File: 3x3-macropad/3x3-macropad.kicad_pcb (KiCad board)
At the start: 2 copper layers, 79.3 x 79.3 mm, 40 parts, among them SW1 SW_Push, SW2 RotaryEncoder_Switch, U1 ATmega32U4-A, Y1 16MHz

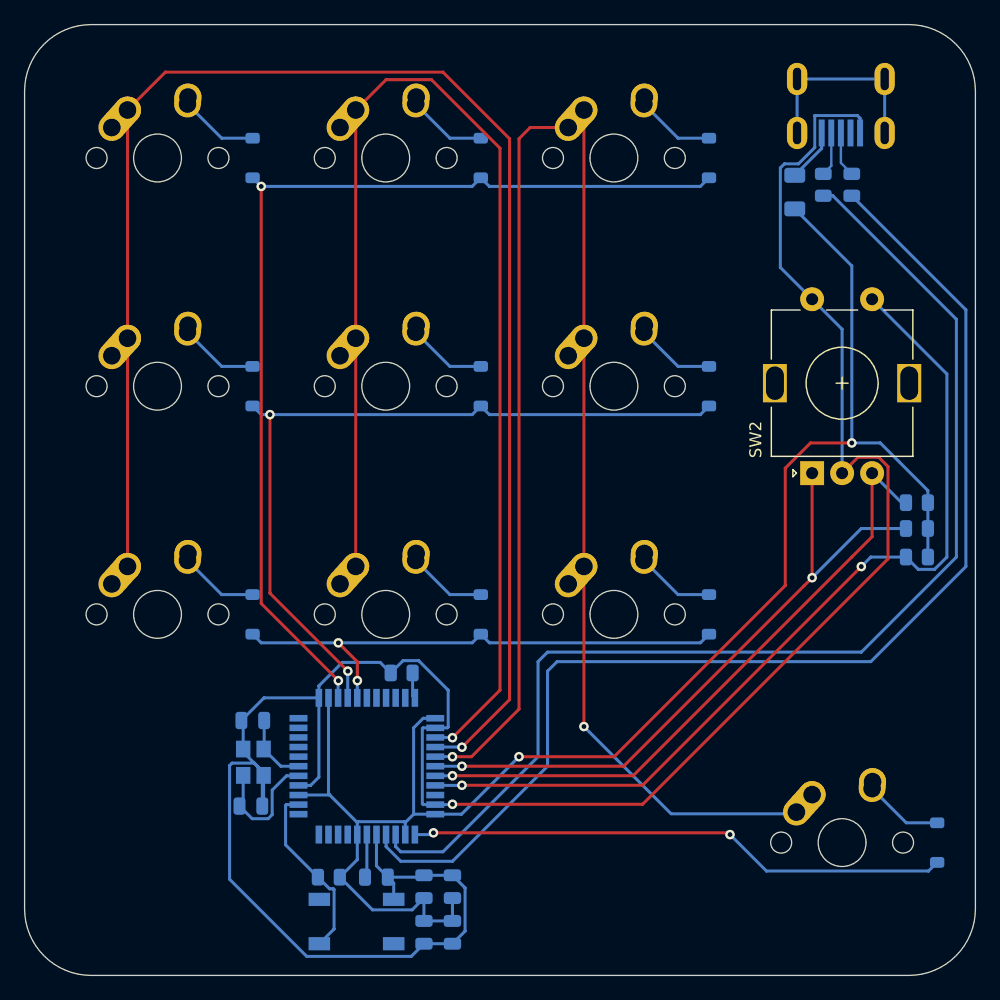
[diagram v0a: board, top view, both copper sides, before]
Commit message: resized 3x3, readied for export to jlcpcb
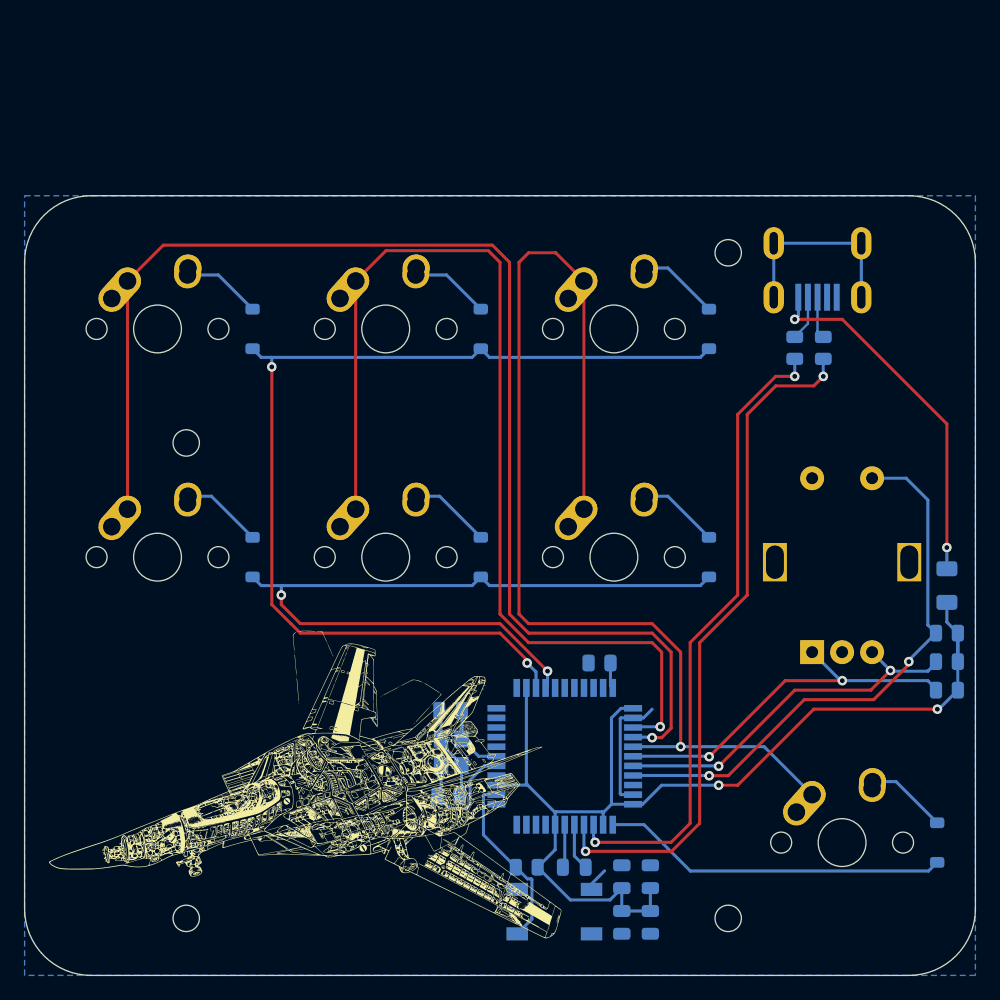
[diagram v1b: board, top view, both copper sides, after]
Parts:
- removed D7, D8, D9: SOD_123, Diode_SMD:D_SOD-123
- removed MX7, MX8, MX9: MX-NoLED, MX_Alps_Hybrid:MX-1U-NoLED
- added G***: LOGO, LOGO, F.Cu at (111.0, 107.8)
- added REF**: MountingHole_2.2mm_M2, MountingHole:MountingHole_2.2mm_M2, F.Cu at (145.9, 118.1)
- added REF**: MountingHole_2.2mm_M2, MountingHole:MountingHole_2.2mm_M2, F.Cu at (145.9, 62.6)
- added REF**: MountingHole_2.2mm_M2, MountingHole:MountingHole_2.2mm_M2, F.Cu at (100.7, 118.1)
- added REF**: MountingHole_2.2mm_M2, MountingHole:MountingHole_2.2mm_M2, F.Cu at (100.7, 78.5)
- moved F1 35.2 mm to (164.1, 90.4)
- moved C2 16.5 mm to (139.4, 114.6)
- moved C7 16.5 mm to (139.4, 118.5)
- moved R4 16.5 mm to (135.1, 96.8)
- moved C1 16.5 mm to (137.0, 114.6)
- moved C3 16.5 mm to (137.0, 118.5)
- moved C4 16.5 mm to (122.7, 100.8)
- moved C5 16.5 mm to (122.6, 107.9)
- moved C6 16.5 mm to (133.0, 113.9)
- moved R3 16.5 mm to (129.1, 113.9)
- moved SW1 16.5 mm to (131.4, 117.6)
- moved Y1 16.5 mm to (122.8, 104.3)
- moved U1 16.5 mm to (132.2, 104.6)
- moved SW2 14.9 mm to (152.9, 95.9)
- moved D1 14.3 mm to (106.2, 69.0)
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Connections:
- D10 pad 1: ROW3 -> ROW2
- U1 pad 1: ROW3 -> ROW2
- U1 pad 27: ROW2 -> unconnected-(U1-PD7-Pad27)
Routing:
- net GND: track 203.6 -> 24.9 mm, vias 1 -> 0
- net +5V: track 139.4 -> 92.2 mm
- net ROW3: track 45.2 -> 0.00 mm, vias 2 -> 0
- net Net-(U1-D-): track 97.9 -> 53.4 mm, vias 0 -> 2
- net COL2: track 142.9 -> 100.3 mm, vias 2 -> 1
- net Net-(U1-D+): track 99.5 -> 57.6 mm, vias 0 -> 2
- net ENCBTN: track 75.5 -> 47.2 mm
- net VCC: track 4.46 -> 30.3 mm, vias 0 -> 2
- net ENCA: track 56.2 -> 31.8 mm
- net COL0: track 134.1 -> 110.7 mm
- net ENCB: track 53.8 -> 31.2 mm, vias 1 -> 2
- net COL1: track 111.7 -> 89.2 mm
- net ROW2: track 44.5 -> 29.0 mm, vias 2 -> 0
- net Net-(D7-A): track 6.61 -> 0.00 mm
- net Net-(D9-A): track 6.61 -> 0.00 mm
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- added copper zone on B.Cu, net GND
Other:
- board size 79.3 x 79.3 mm -> 79.3 x 65 mm

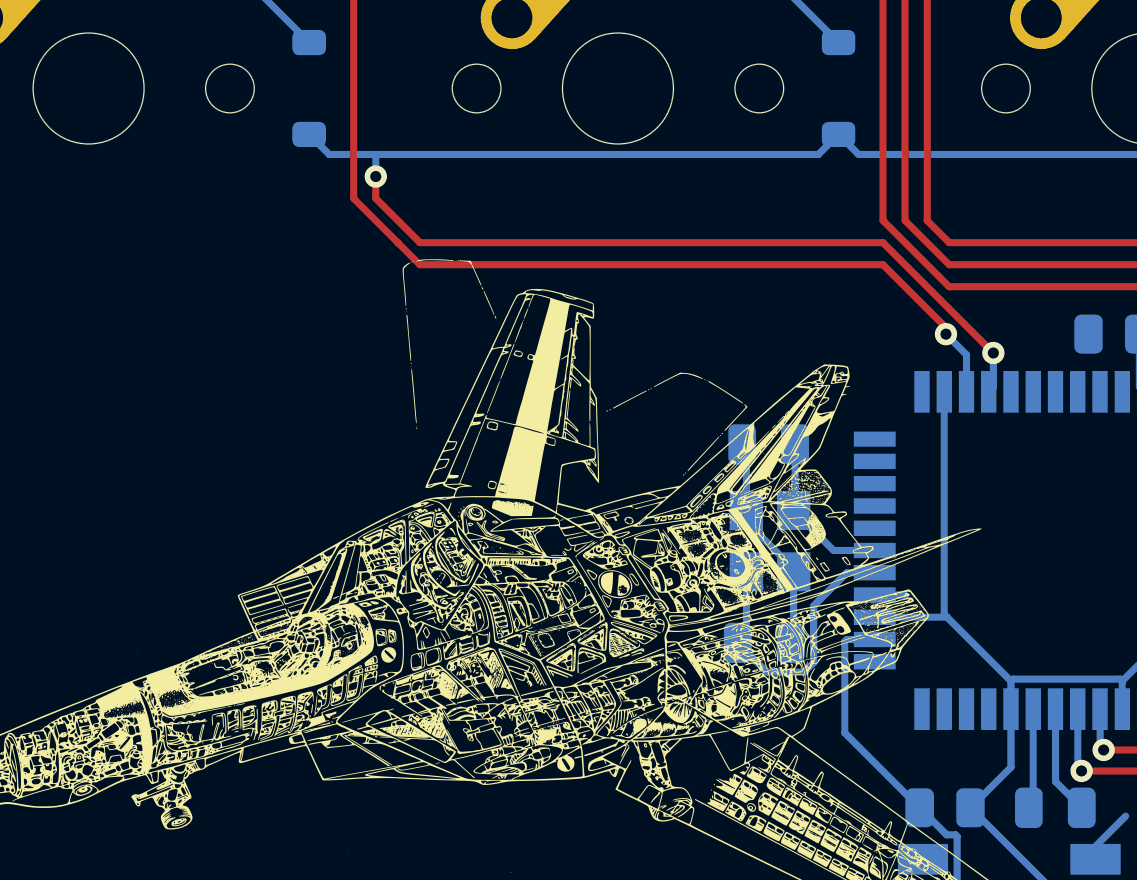
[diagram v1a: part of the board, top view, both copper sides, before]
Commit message: add isp flashing breakout
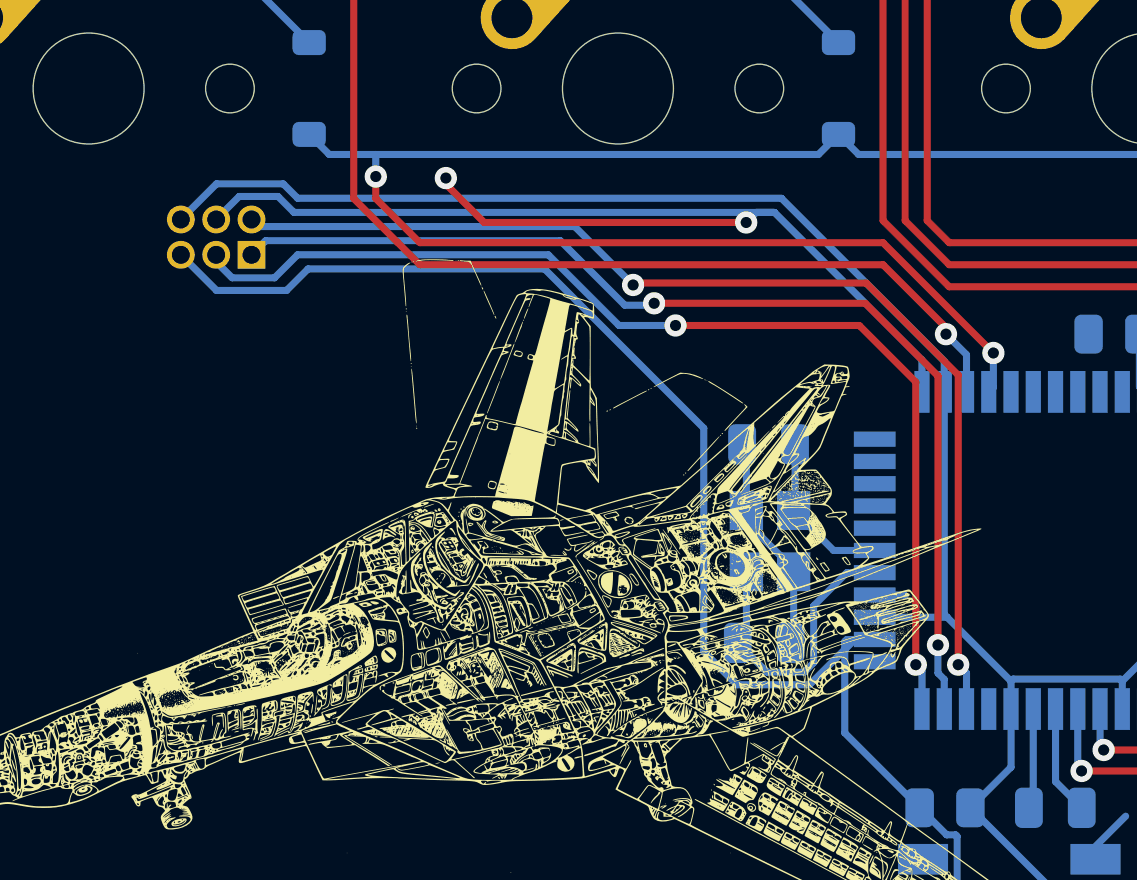
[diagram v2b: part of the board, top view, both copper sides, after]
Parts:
- added J1: Conn_02x03_Counter_Clockwise, Connector_PinHeader_1.27mm:PinHeader_2x03_P1.27mm_Horizontal, B.Cu at (104.1, 94.0)
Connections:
- net Net-(U1-~{RESET}) renamed RESET
- U1 pad 10: unconnected-(U1-PB2-Pad10) -> MOSI
- U1 pad 11: unconnected-(U1-PB3-Pad11) -> MISO
- U1 pad 9: unconnected-(U1-PB1-Pad9) -> SCLK
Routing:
- net GND: track 24.9 -> 66.9 mm, vias 0 -> 2
- net SCLK: track 0.00 -> 39.9 mm, vias 0 -> 2
- net MISO: track 0.00 -> 39.7 mm, vias 0 -> 2
- net MOSI: track 0.00 -> 39.0 mm, vias 0 -> 2
- net RESET: track 15.0 -> 52.4 mm
- net +5V: track 92.2 -> 123.9 mm
